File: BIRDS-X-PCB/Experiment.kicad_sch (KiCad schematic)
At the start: 27 parts, among them U1 LM334M, U2 ADG734, U3 LM334M, U301 VT01, U302 LM335DT, U303 LM335DT, U304 VT01, U305 VT01, U306 VT01, U307 LM335DT, U308 LM335DT, U309 LM335DT, U4 LM334M, U5 LM334M

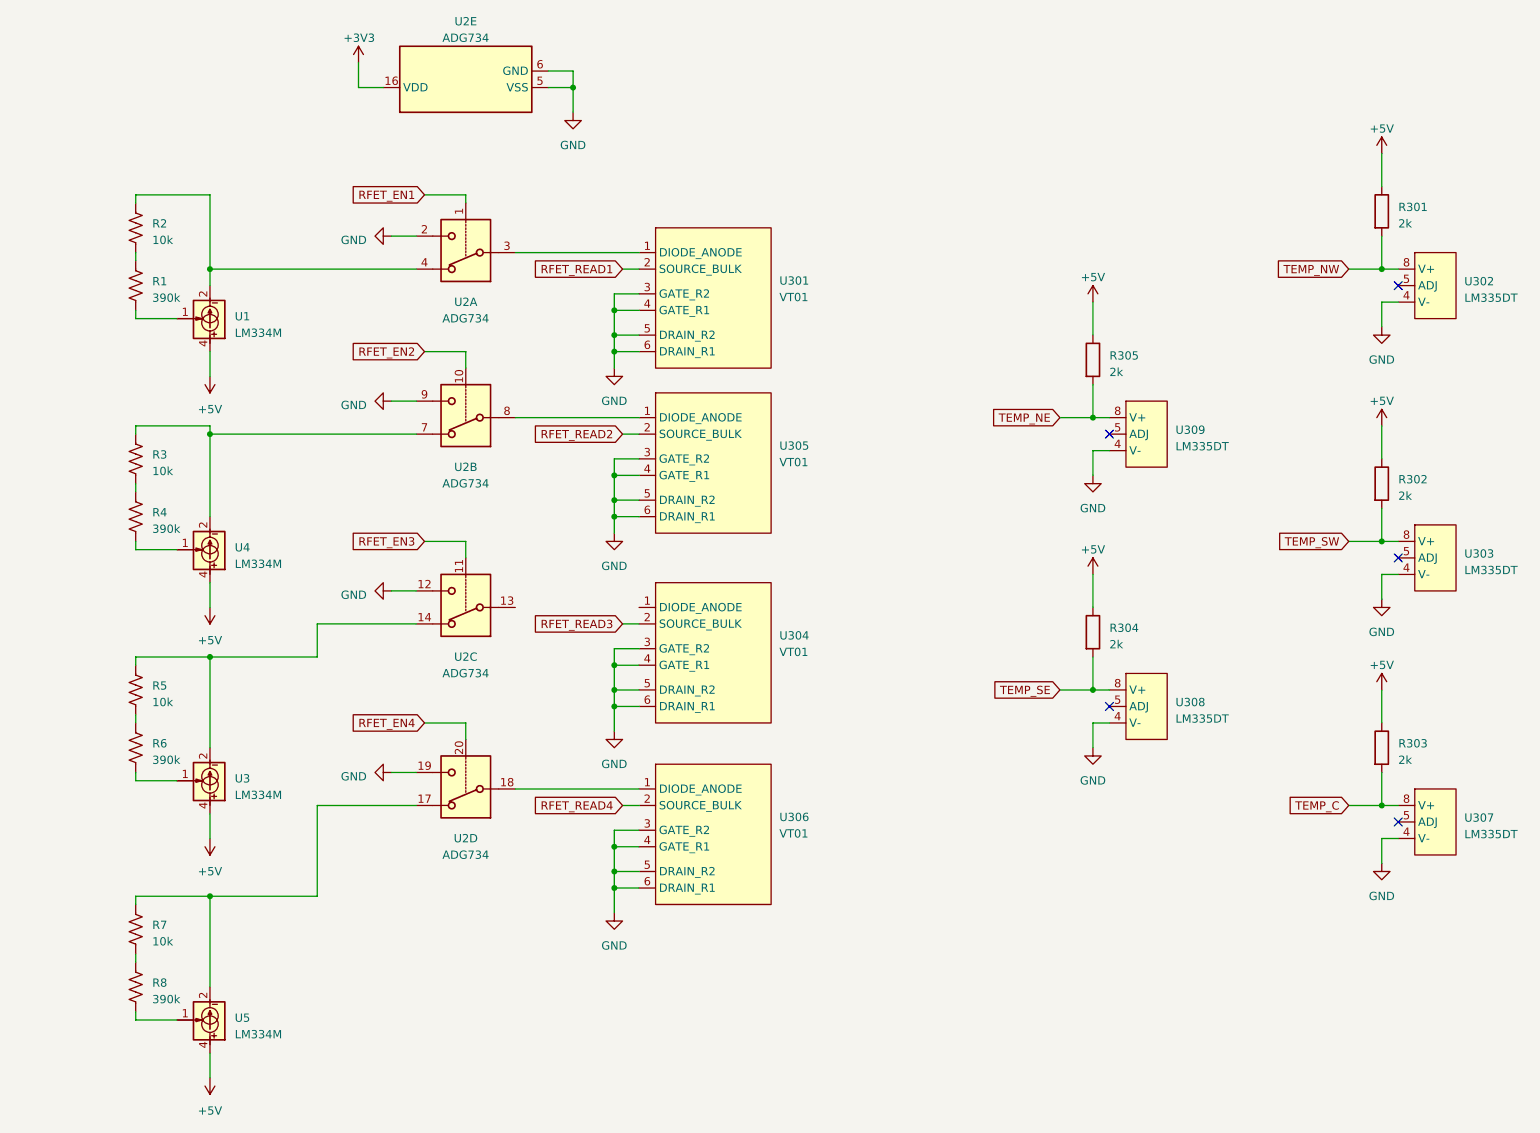
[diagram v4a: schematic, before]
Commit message: Completed MCU & Experiment Circuit
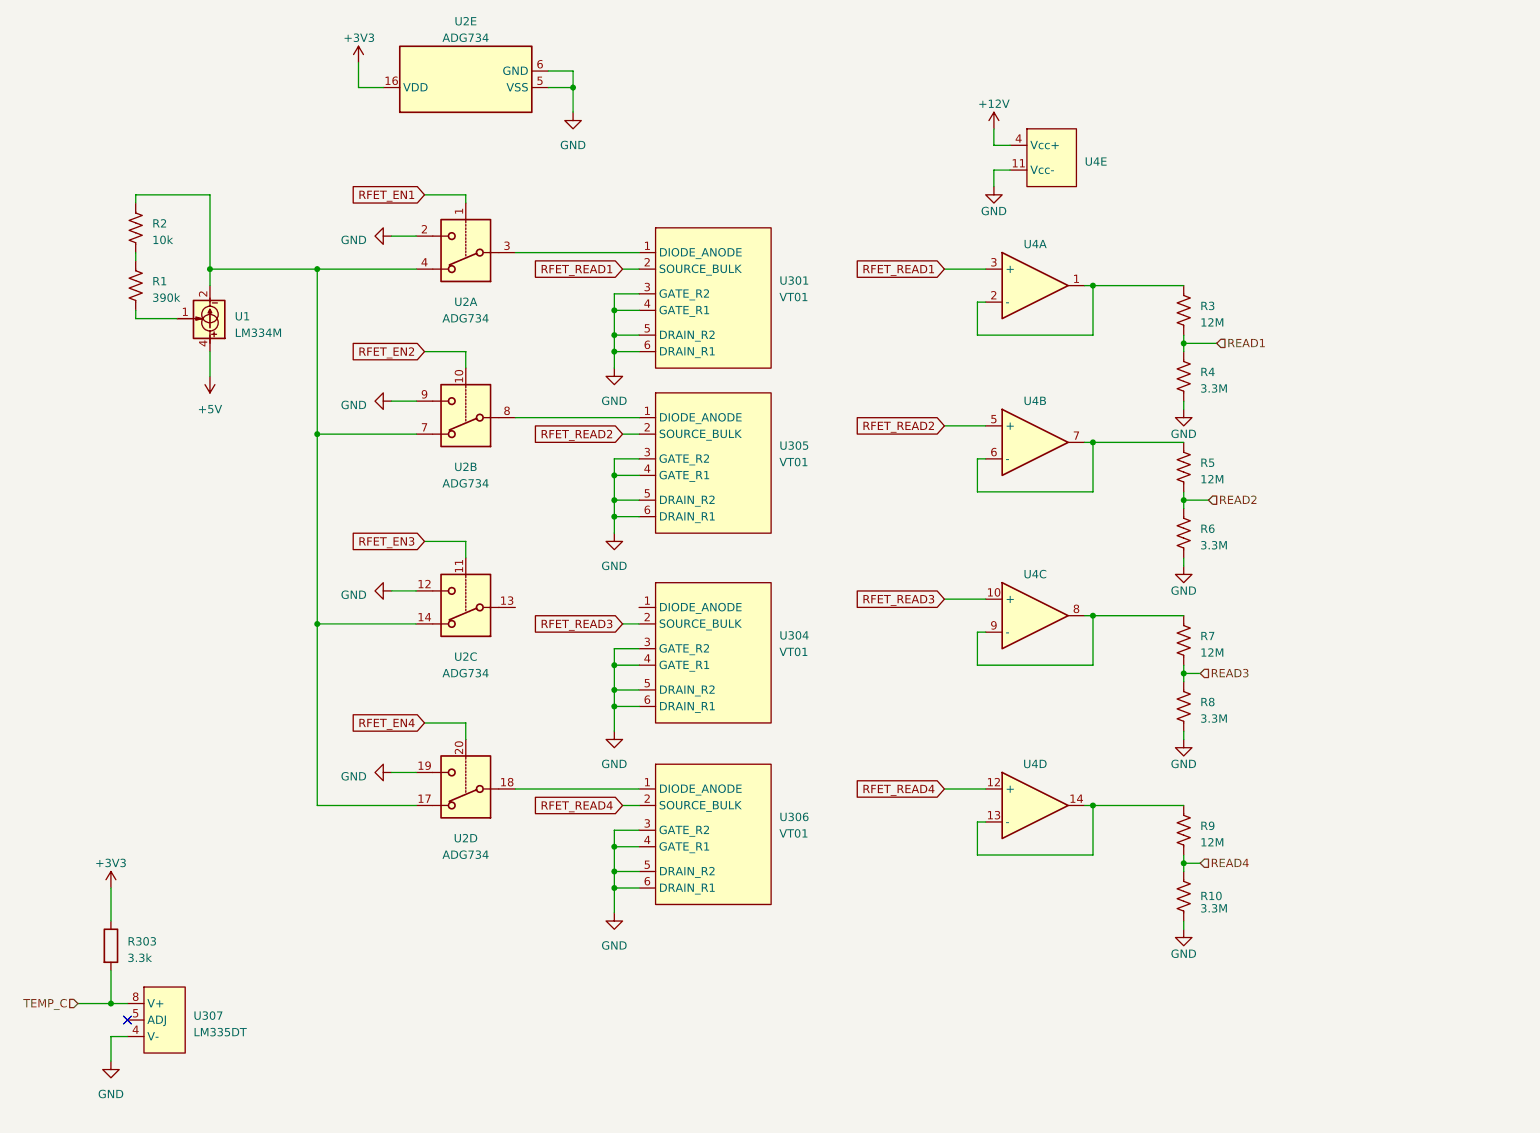
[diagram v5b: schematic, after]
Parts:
- removed R301, R302, R304, R305: 2k, Resistor_SMD:R_1206_3216Metric_Pad1.30x1.75mm_HandSolder, symbol Device:R
- removed U3, U4, U5: LM334M, Package_SO:SOIC-8_3.9x4.9mm_P1.27mm, symbol Reference_Current:LM334M
- removed U302, U303, U308, U309: LM335DT, Package_SO:SOIC-8_3.9x4.9mm_P1.27mm, symbol BIRDS-X_Symbols_Lib:LM335DT
- added R10: 3.3M, Resistor_SMD:R_1206_3216Metric, symbol Device:R_US
- added R9: 12M, Resistor_SMD:R_1206_3216Metric, symbol Device:R_US
- added U4: ~, lib:SOP65P640X120-14N, symbol BIRDS-X_Symbols_Lib:TL974IPWR
- R3, R5, R7: value 10k -> 12M
- R303: value 2k -> 3.3k
- R4, R6, R8: value 390k -> 3.3M
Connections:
- net +3V3: now also R303.1
- net +5V: no longer R303.1
- net GND: now also R4.2, R6.2, R8.2, R10.2, U4.11 (Vcc-)
- net RFET_READ1: now also U4.3 (+)
- net RFET_READ2: now also U4.5 (+)
- net RFET_READ3: now also U4.10 (+)
- net RFET_READ4: now also U4.12 (+)
- net READ3: now reaches R7.2, R8.1
- net READ1: now reaches R3.2, R4.1
- net at R2.1, U1.2, U1.3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: now also U2.14, U2.17, U2.7
- net at R5.1: now also U4.6 (-), U4.7; no longer U2.14
- net at R7.1: now also U4.8, U4.9 (-); no longer U2.17
- net at R3.1: now also U4.1, U4.2 (-); no longer U2.7
- net READ2: now reaches R5.2, R6.1
- new net: R9.1, U4.13 (-), U4.14
- new net +12V: U4.4 (Vcc+)
- new net READ4: R10.1, R9.2
- no-connect marks 5 -> 1
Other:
- moved on the sheet: R303, U307

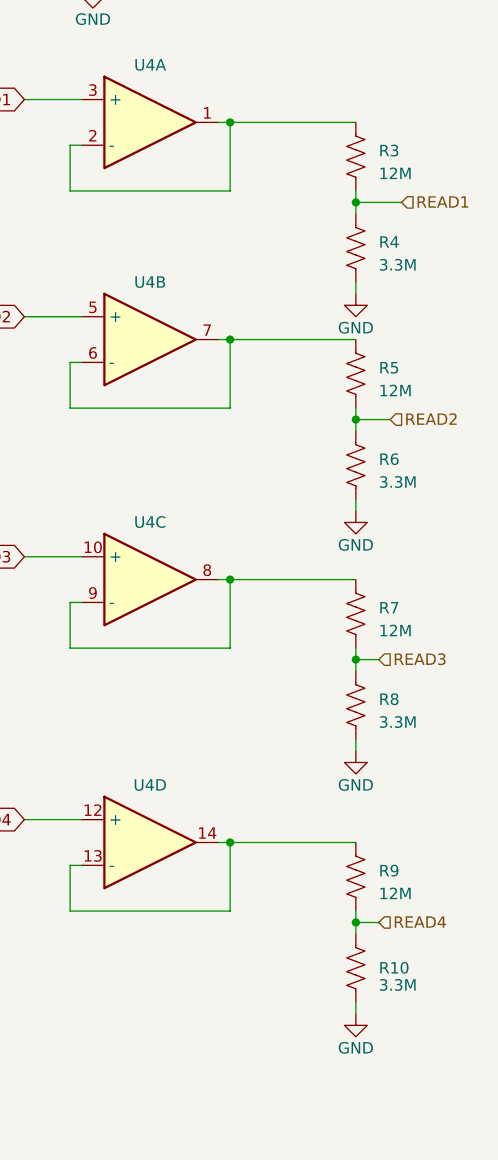
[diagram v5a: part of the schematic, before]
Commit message: Fixed voltage dividers
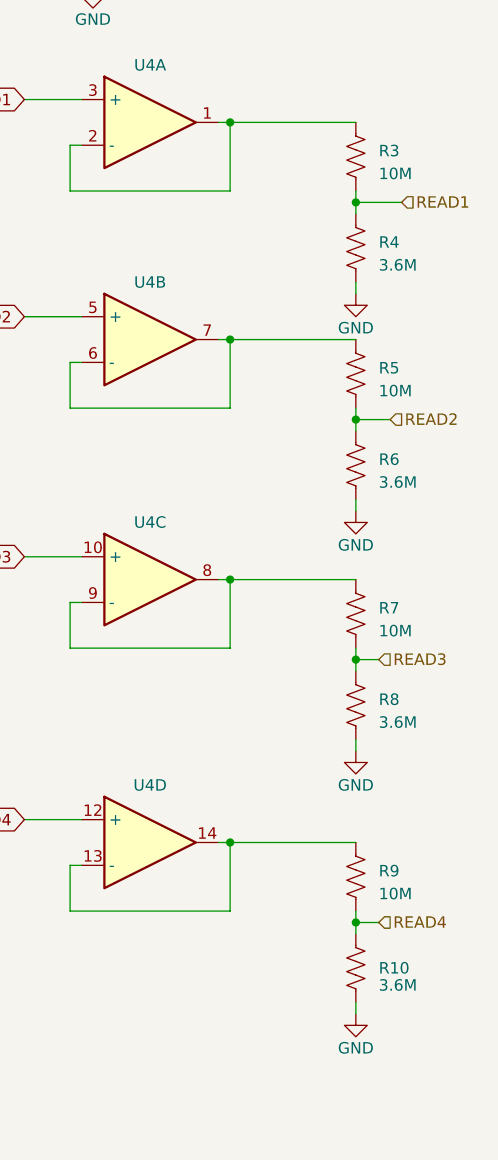
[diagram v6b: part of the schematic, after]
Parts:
- R10, R4, R6, R8: value 3.3M -> 3.6M
- R3, R5, R7, R9: value 12M -> 10M
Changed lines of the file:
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@@
       (effects (font (size 1.27 1.27)) (justify left))
     )
-    (property "Value" "12M" (at 212.09 67.945 0)
+    (property "Value" "10M" (at 212.09 67.945 0)
       (effects (font (size 1.27 1.27)) (justify left))
     )
@@
       (effects (font (size 1.27 1.27)) (justify left))
     )
-    (property "Value" "3.3M" (at 212.09 158.115 0)
+    (property "Value" "3.6M" (at 212.09 158.115 0)
       (effects (font (size 1.27 1.27)) (justify left))
     )
@@
       (effects (font (size 1.27 1.27)) (justify left))
     )
-    (property "Value" "12M" (at 212.09 92.075 0)
+    (property "Value" "10M" (at 212.09 92.075 0)
       (effects (font (size 1.27 1.27)) (justify left))
     )
@@
       (effects (font (size 1.27 1.27)) (justify left))
     )
-    (property "Value" "12M" (at 212.09 118.745 0)
+    (property "Value" "10M" (at 212.09 118.745 0)
       (effects (font (size 1.27 1.27)) (justify left))
     )
@@
       (effects (font (size 1.27 1.27)) (justify left))
     )
-    (property "Value" "3.3M" (at 212.09 102.235 0)
+    (property "Value" "3.6M" (at 212.09 102.235 0)
       (effects (font (size 1.27 1.27)) (justify left))
     )
@@
       (effects (font (size 1.27 1.27)) (justify left))
     )
-    (property "Value" "12M" (at 212.09 147.955 0)
+    (property "Value" "10M" (at 212.09 147.955 0)
       (effects (font (size 1.27 1.27)) (justify left))
     )
@@
       (effects (font (size 1.27 1.27)) (justify left))
     )
-    (property "Value" "3.3M" (at 212.09 128.905 0)
+    (property "Value" "3.6M" (at 212.09 128.905 0)
       (effects (font (size 1.27 1.27)) (justify left))
     )
@@
       (effects (font (size 1.27 1.27)) (justify left))
     )
-    (property "Value" "3.3M" (at 212.09 78.105 0)
-      (effects (font (size 1.27 1.27)) (justify left))
-    )
+    (property "Value" "3.6M" (at 212.09 78.105 0)
+      (effects (font (size 1.27 1.27)) (justify left))
+    )

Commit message: Add TODO and update PDF
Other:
- note added: "TODO update this symbol to add a part label"
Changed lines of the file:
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@@
     (stroke (width 0) (type default))
+  )
+  (text "TODO update this symbol to add a part label" (at 170.18 33.02 0)
+    (effects (font (size 1.27 1.27)) (justify left bottom))
   )
   (global_label "RFET_READ1" (shape input) (at 172.72 59.69 180) (fields_autoplaced)

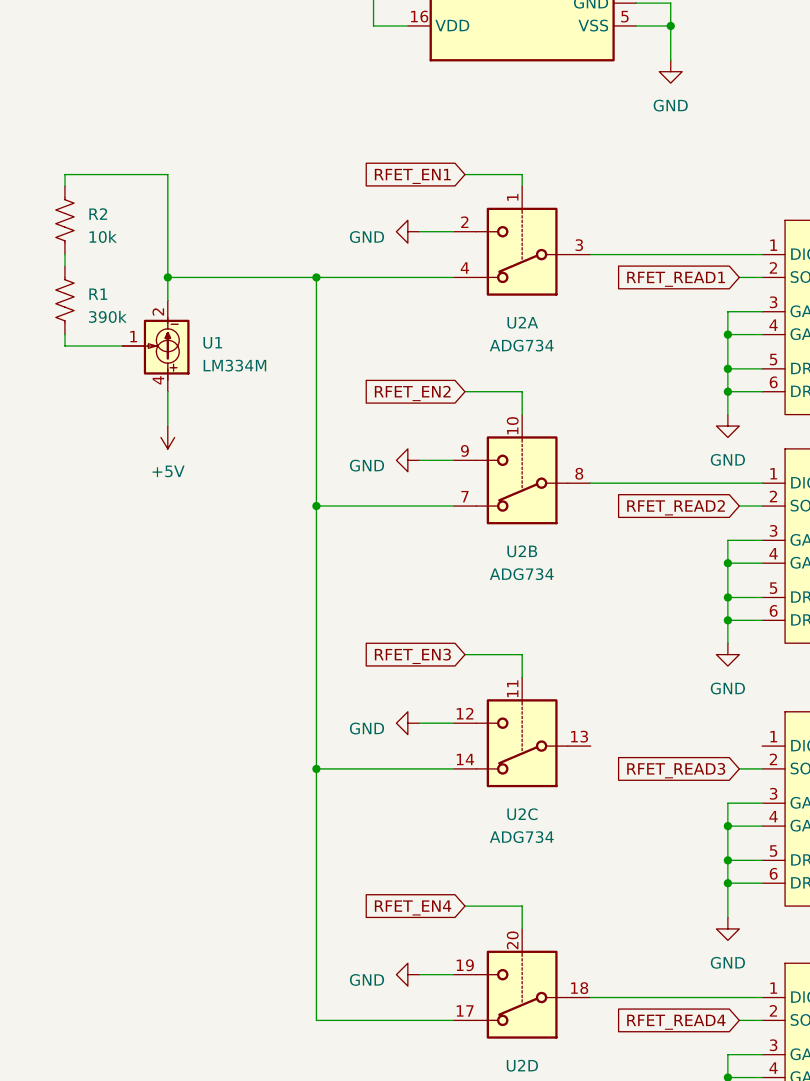
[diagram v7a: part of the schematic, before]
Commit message: Added RFET enabling connections
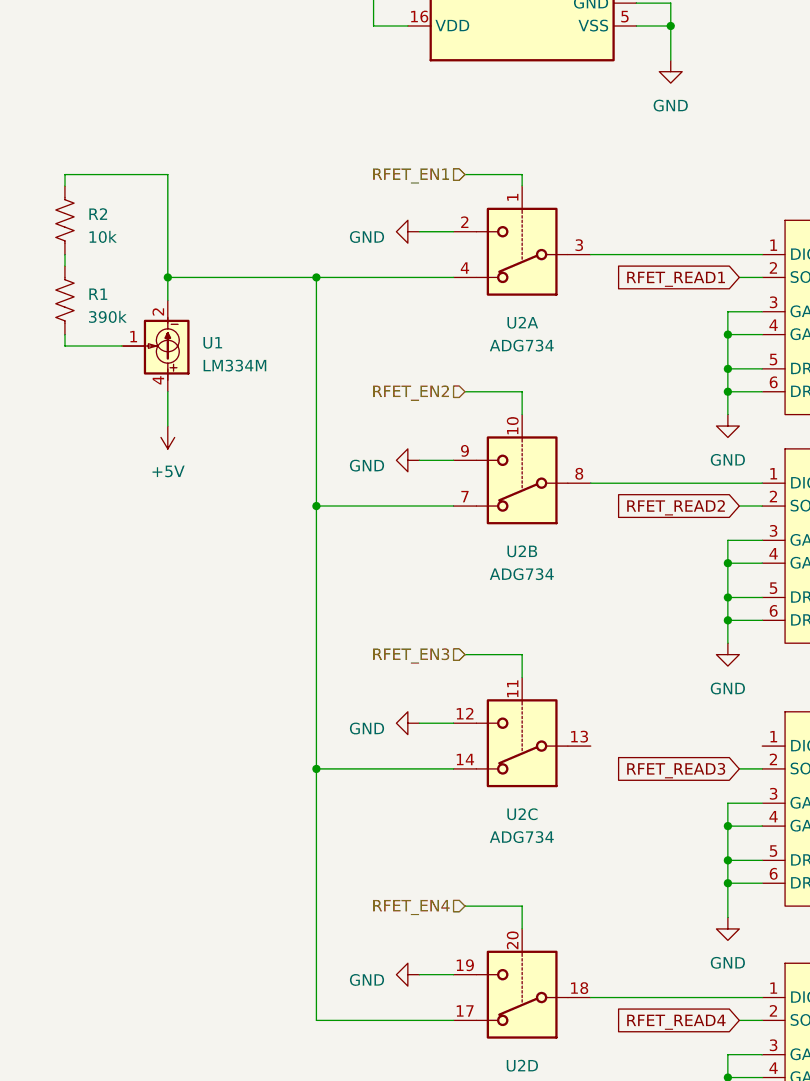
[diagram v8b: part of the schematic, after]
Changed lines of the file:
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@@
-    )
-  )
-  (global_label "RFET_EN3" (shape input) (at 92.71 101.6 180) (fields_autoplaced)
-    (effects (font (size 1.27 1.27)) (justify right))
-    (property "Intersheetrefs" "${INTERSHEET_REFS}" (at 80.6724 101.6 0)
-      (effects (font (size 1.27 1.27)) (justify right) hide)
     )
   )
@@
     )
   )
-  (global_label "RFET_EN4" (shape input) (at 92.71 129.54 180) (fields_autoplaced)
-    (effects (font (size 1.27 1.27)) (justify right))
-    (property "Intersheetrefs" "${INTERSHEET_REFS}" (at 80.6724 129.54 0)
-      (effects (font (size 1.27 1.27)) (justify right) hide)
-    )
-  )
   (global_label "RFET_READ3" (shape input) (at 123.19 114.3 180) (fields_autoplaced)
     (effects (font (size 1.27 1.27)) (justify right))
@@
     (effects (font (size 1.27 1.27)) (justify right))
     (property "Intersheetrefs" "${INTERSHEET_REFS}" (at 158.3843 83.82 0)
-      (effects (font (size 1.27 1.27)) (justify right) hide)
-    )
-  )
-  (global_label "RFET_EN2" (shape input) (at 92.71 72.39 180) (fields_autoplaced)
-    (effects (font (size 1.27 1.27)) (justify right))
-    (property "Intersheetrefs" "${INTERSHEET_REFS}" (at 80.6724 72.39 0)
-      (effects (font (size 1.27 1.27)) (justify right) hide)
-    )
-  )
-  (global_label "RFET_EN1" (shape input) (at 92.71 48.26 180) (fields_autoplaced)
-    (effects (font (size 1.27 1.27)) (justify right))
-    (property "Intersheetrefs" "${INTERSHEET_REFS}" (at 80.6724 48.26 0)
       (effects (font (size 1.27 1.27)) (justify right) hide)
     )
@@
     )
   )
+  (hierarchical_label "RFET_EN4" (shape input) (at 92.71 129.54 180) (fields_autoplaced)
+    (effects (font (size 1.27 1.27)) (justify right))
+  )
+  (hierarchical_label "RFET_EN1" (shape input) (at 92.71 48.26 180) (fields_autoplaced)
+    (effects (font (size 1.27 1.27)) (justify right))
+  )
   (hierarchical_label "READ4" (shape input) (at 212.09 151.13 0) (fields_autoplaced)
     (effects (font (size 1.27 1.27)) (justify left))
@@
     (effects (font (size 1.27 1.27)) (justify left))
   )
+  (hierarchical_label "RFET_EN2" (shape input) (at 92.71 72.39 180) (fields_autoplaced)
+    (effects (font (size 1.27 1.27)) (justify right))
+  )
+  (hierarchical_label "RFET_EN3" (shape input) (at 92.71 101.6 180) (fields_autoplaced)
+    (effects (font (size 1.27 1.27)) (justify right))
+  )
   (hierarchical_label "TEMP_C" (shape input) (at 39.37 172.72 180) (fields_autoplaced)
